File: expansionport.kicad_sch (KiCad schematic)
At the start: 0 parts

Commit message: place expansion port and set footprint
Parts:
- added J?: C64_Expansion_Port, HackupNet:C64-Cart-Socket-Vertical, symbol 00Project-TapePort:C64_Expansion_Port
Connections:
- new net +5V: J?.2 (Pin_2), J?.3 (Pin_3)
- new net A0: J?.Y (Pin_Y)
- new net A1: J?.X (Pin_X)
- new net A10: J?.M (Pin_M)
- new net A11: J?.L (Pin_L)
- new net A12: J?.K (Pin_K)
- new net A13: J?.J (Pin_J)
- new net A14: J?.H (Pin_H)
- new net A15: J?.F (Pin_F)
- new net A2: J?.W (Pin_W)
- new net A3: J?.V (Pin_V)
- new net A4: J?.U (Pin_U)
- new net A5: J?.T (Pin_T)
- new net A6: J?.S (Pin_S)
- new net A7: J?.R (Pin_R)
- new net A8: J?.P (Pin_P)
- new net A9: J?.N (Pin_N)
- new net BA: J?.12 (Pin_12)
- new net D0: J?.21 (Pin_21)
- new net D1: J?.20 (Pin_20)
- new net D2: J?.19 (Pin_19)
- new net D3: J?.18 (Pin_18)
- new net D4: J?.17 (Pin_17)
- new net D5: J?.16 (Pin_16)
- new net D6: J?.15 (Pin_15)
- new net D7: J?.14 (Pin_14)
- new net DMA_N: J?.13 (Pin_13)
- new net DOTCLOCK: J?.6 (Pin_6)
- new net EXROM_N: J?.9 (Pin_9)
- new net GAME_N: J?.8 (Pin_8)
- new net GND: J?.1 (Pin_1), J?.22 (Pin_22), J?.A (Pin_A), J?.Z (Pin_Z)
- new net IO1_N: J?.7 (Pin_7)
- new net IO2_N: J?.10 (Pin_10)
- new net IRQ_N: J?.4 (Pin_4)
- new net NMI_N: J?.D (Pin_D)
- new net PHI2: J?.E (Pin_E)
- new net RESET_N: J?.C (Pin_C)
- new net ROMH_N: J?.B (Pin_B)
- new net ROML_N: J?.11 (Pin_11)
- new net R_W: J?.5 (Pin_5)

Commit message: work on expansion port
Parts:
- added RN? (x4): 3.3K x 8, Resistor_THT:R_Array_SIP9, symbol Device:R_Network08
- added RN?: 4609X-AP1-332LF 3.3Kx8, Resistor_THT:R_Array_SIP9, symbol Device:R_Network08
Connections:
- net +5V: now also RN?.1 (common), RN?.1 (common), RN?.1 (common), RN?.1 (common), RN?.1 (common)
- net A0: now also RN?.9 (R8)
- net A1: now also RN?.8 (R7)
- net A10: now also RN?.7 (R6)
- net A11: now also RN?.6 (R5)
- net A12: now also RN?.5 (R4)
- net A13: now also RN?.4 (R3)
- net A14: now also RN?.3 (R2)
- net A15: now also RN?.2 (R1)
- net A2: now also RN?.7 (R6)
- net A3: now also RN?.6 (R5)
- net A4: now also RN?.5 (R4)
- net A5: now also RN?.4 (R3)
- net A6: now also RN?.3 (R2)
- net A7: now also RN?.2 (R1)
- net A8: now also RN?.9 (R8)
- net A9: now also RN?.8 (R7)
- net BA: now also RN?.9 (R8)
- net D0: now also RN?.2 (R1)
- net D1: now also RN?.3 (R2)
- net D2: now also RN?.4 (R3)
- net D3: now also RN?.5 (R4)
- net D4: now also RN?.6 (R5)
- net D5: now also RN?.7 (R6)
- net D6: now also RN?.8 (R7)
- net D7: now also RN?.9 (R8)
- net DMA_N: now also RN?.8 (R7)
- net EXROM_N: now also RN?.4 (R3)
- net GAME_N: now also RN?.5 (R4)
- net IO1_N: now also RN?.6 (R5)
- net IO2_N: now also RN?.3 (R2)
- net IRQ_N: now also RN?.9 (R8)
- net NMI_N: now also RN?.5 (R4)
- net PHI2: now also RN?.4 (R3)
- net RESET_N: now also RN?.6 (R5)
- net ROMH_N: now also RN?.7 (R6)
- net ROML_N: now also RN?.2 (R1)
- net R_W: now also RN?.8 (R7)
- no-connect marks 0 -> 3
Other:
- note added: "DOTCLOCK is directly from the FPGA through a level converter only, to get the required speed. All other signals, including CLK and R/W can be driven through the MUX bus. CLK, R_W, ROMH, ROML, IO1 and IO2 should be driven simultaneously to ensure clean address decoding."
- note added: "DOTCLOCK, IO1_N, IO2_N, ROML_N, ROMH_N, BA, PHI2 are all output only, and expect CMOS signals. IRQ_N, GAME_N, EXROM_N, NMI_N, DMA_N, RESET_N are all input only. IRQ, NMI and R/W can be open-collector outputs, with 3.3K pull-ups to match the C64. Thus we can use our normal mux latching with those signals. D0-7 and A0-15 are bidirectional, but direction switched as two banks. These can use 74LS244s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"

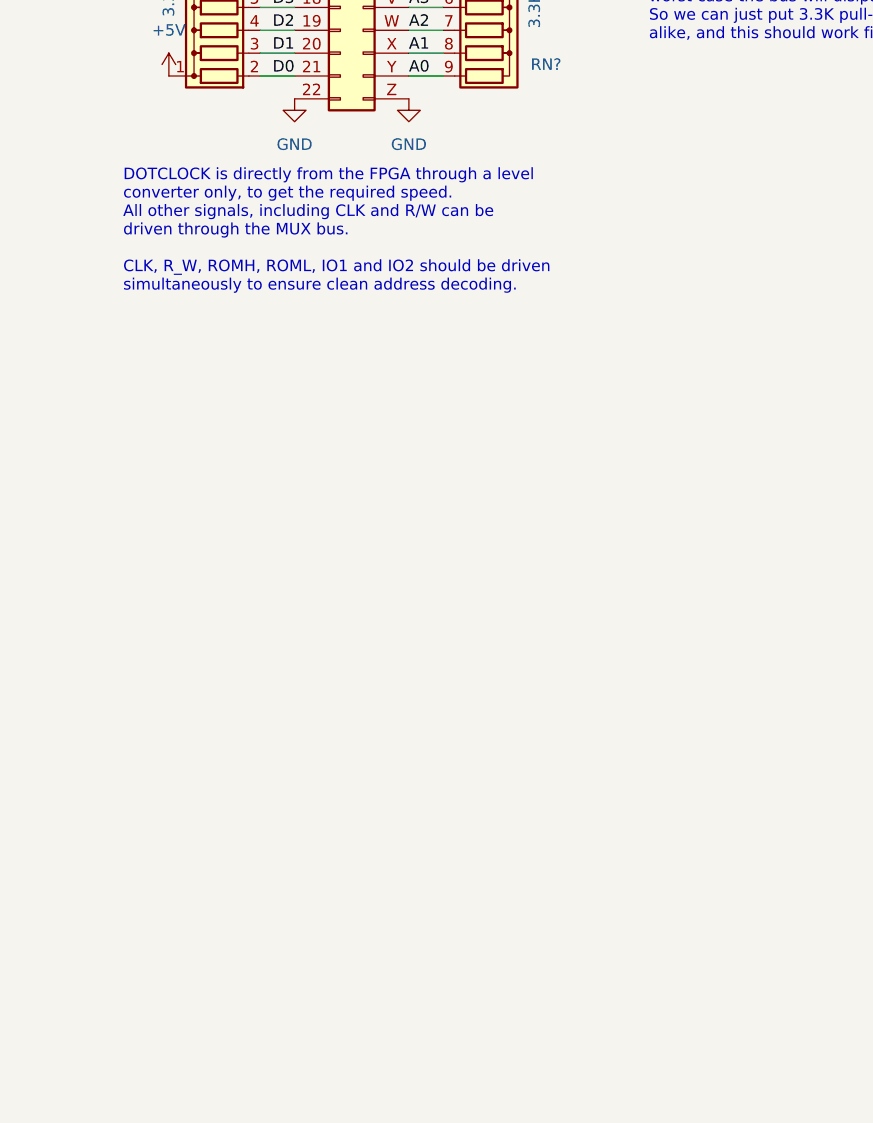
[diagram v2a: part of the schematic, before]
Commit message: DOTCLOCK fed via 74LS04 to perform fast level conversion
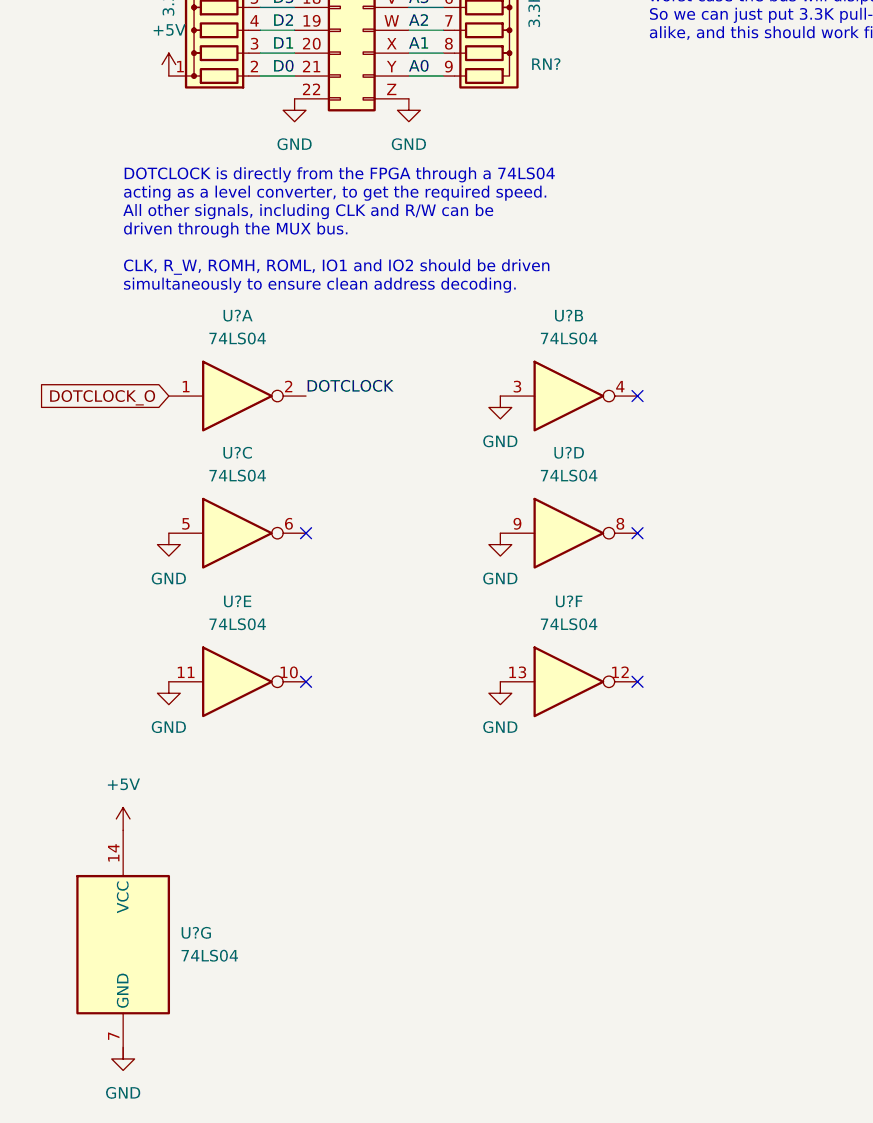
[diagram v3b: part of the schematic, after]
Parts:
- added U? (x7): 74LS04, symbol 74xx:74LS04
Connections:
- net +5V: now also U?.14 (VCC)
- net DOTCLOCK: now also U?.2
- net GND: now also U?.11, U?.13, U?.3, U?.5, U?.9
- new net DOTCLOCK_O: U?.1
- no-connect marks 3 -> 8
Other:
- note added: "DOTCLOCK is directly from the FPGA through a 74LS04 acting as a level converter, to get the required speed. All other signals, including CLK and R/W can be driven through the MUX bus. CLK, R_W, ROMH, ROML, IO1 and IO2 should be driven simultaneously to ensure clean address decoding."
- note removed: "DOTCLOCK is directly from the FPGA through a level converter only, to get the required speed. All other signals, including CLK and R/W can be driven through the MUX bus. CLK, R_W, ROMH, ROML, IO1 and IO2 should be driven simultaneously to ensure clean address decoding."

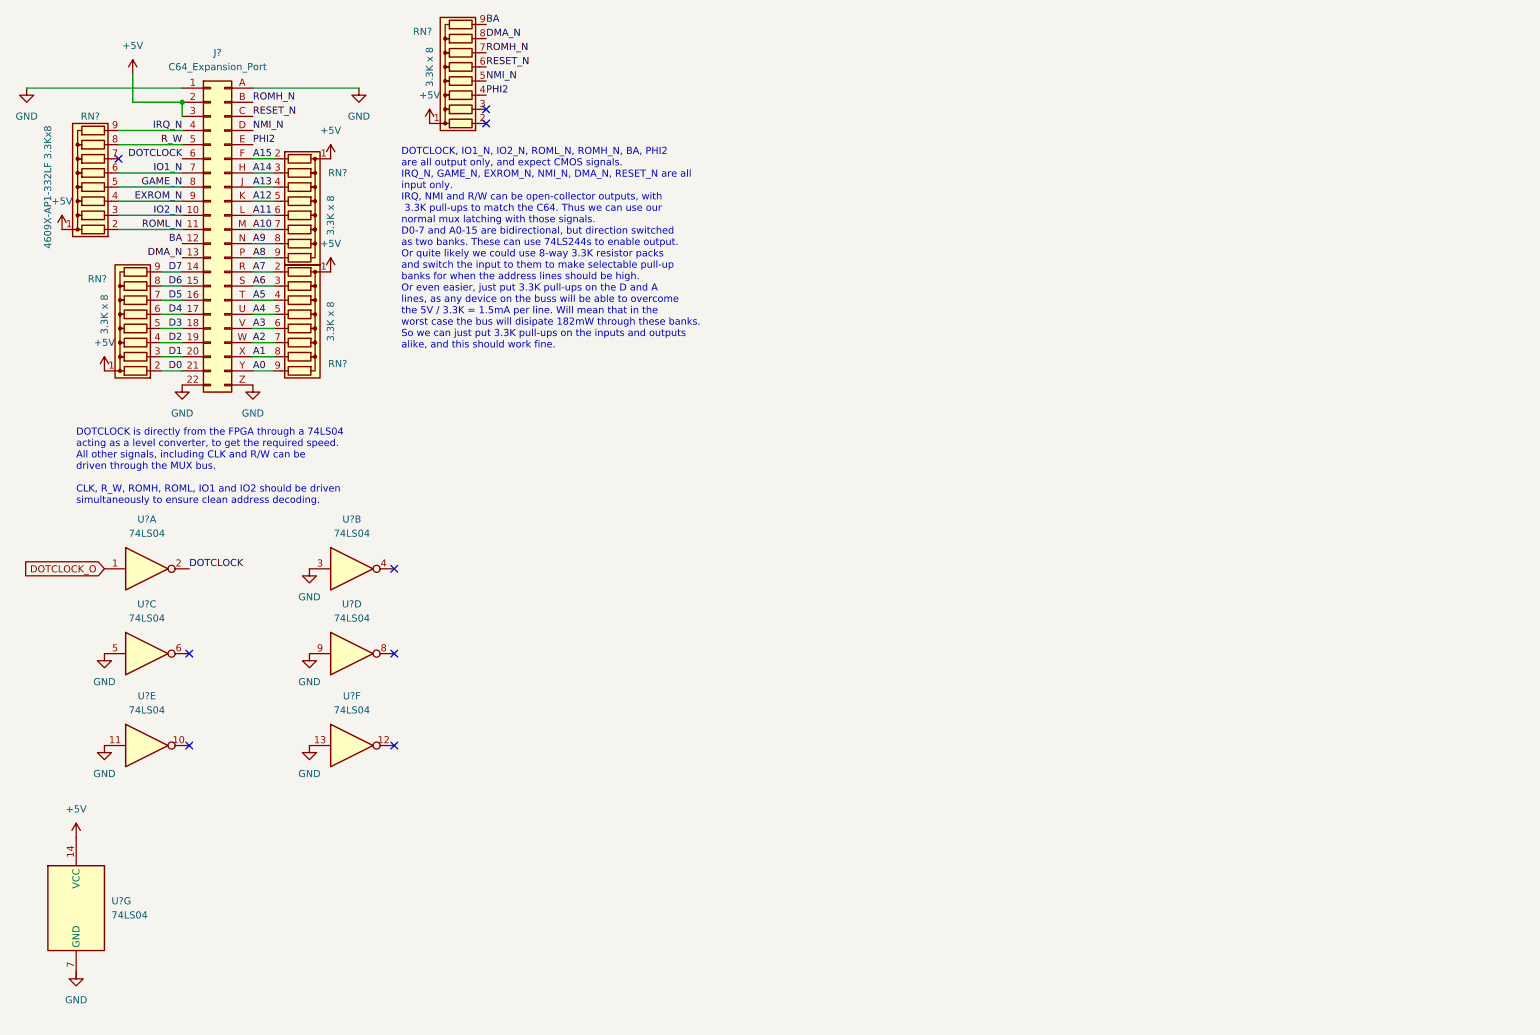
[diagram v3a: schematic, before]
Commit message: hook up expansion port using MUX bus
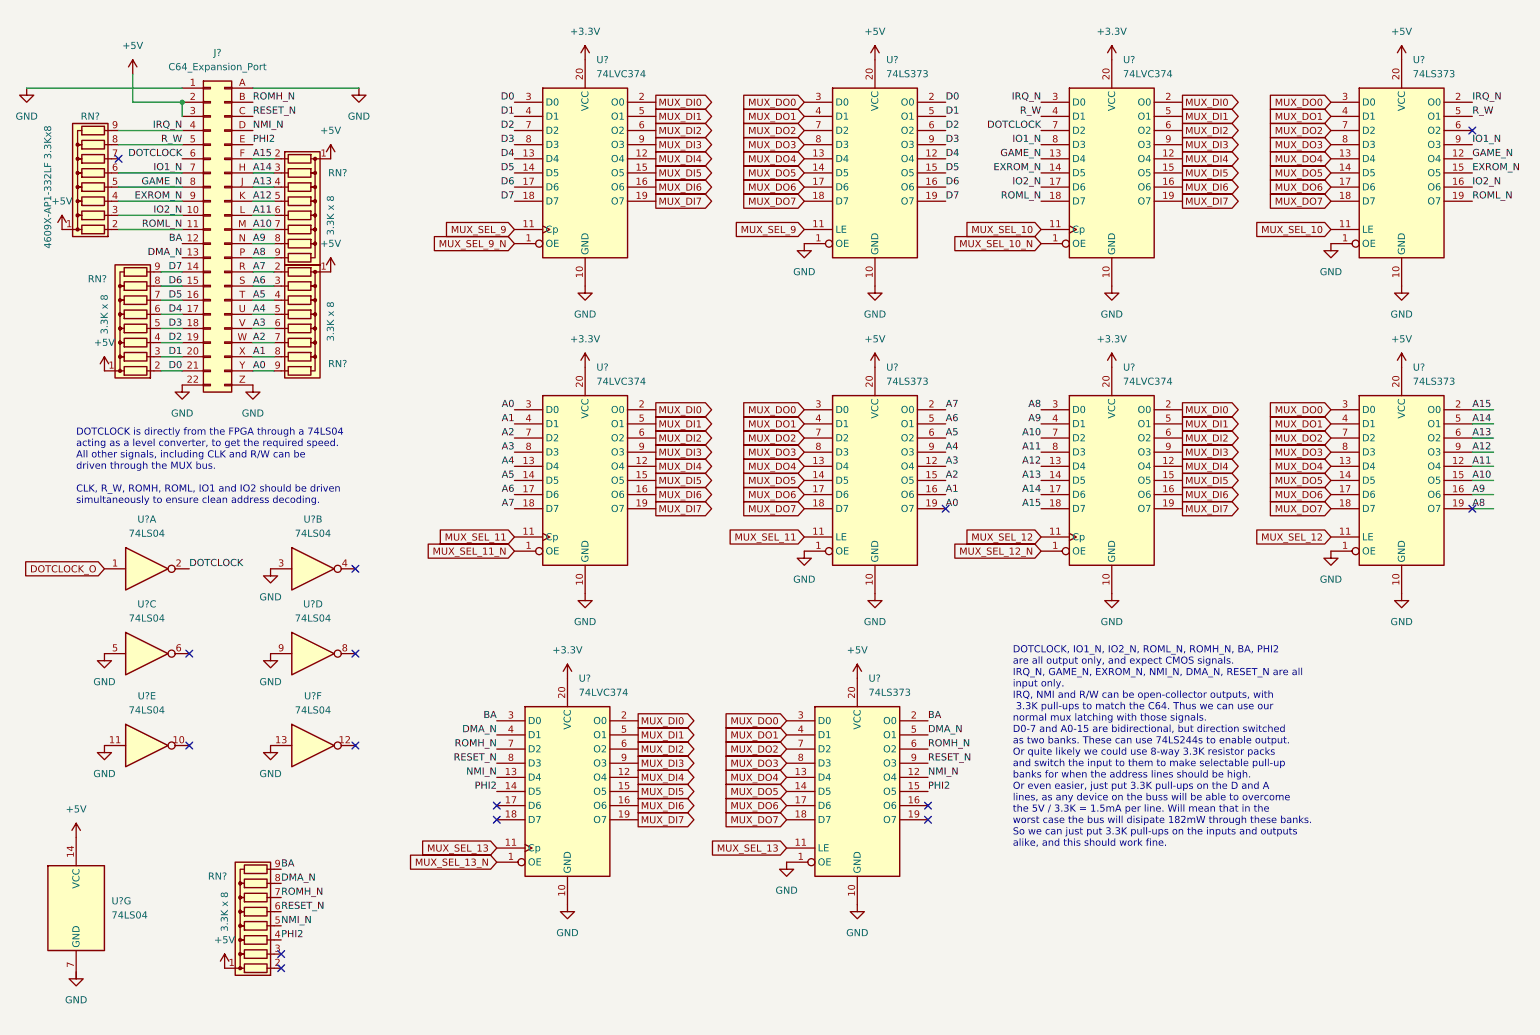
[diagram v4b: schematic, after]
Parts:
- added U? (x5): 74LS373, Package_DIP:DIP-20_W7.62mm, symbol 74xx:74LS373
- added U? (x5): 74LVC374, Package_DIP:DIP-20_W7.62mm, symbol 74xx:74HC374
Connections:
- net +5V: now also U?.20 (VCC), U?.20 (VCC), U?.20 (VCC), U?.20 (VCC), U?.20 (VCC)
- net A0: now also U?.19 (O7), U?.3 (D0)
- net A1: now also U?.16 (O6), U?.4 (D1)
- net A10: now also U?.15 (O5), U?.7 (D2)
- net A11: now also U?.12 (O4), U?.8 (D3)
- net A12: now also U?.13 (D4), U?.9 (O3)
- net A13: now also U?.14 (D5), U?.6 (O2)
- net A14: now also U?.17 (D6), U?.5 (O1)
- net A15: now also U?.18 (D7), U?.2 (O0)
- net A2: now also U?.15 (O5), U?.7 (D2)
- net A3: now also U?.12 (O4), U?.8 (D3)
- net A4: now also U?.13 (D4), U?.9 (O3)
- net A5: now also U?.14 (D5), U?.6 (O2)
- net A6: now also U?.17 (D6), U?.5 (O1)
- net A7: now also U?.18 (D7), U?.2 (O0)
- net A8: now also U?.19 (O7), U?.3 (D0)
- net A9: now also U?.16 (O6), U?.4 (D1)
- net BA: now also U?.2 (O0), U?.3 (D0)
- net D0: now also U?.2 (O0), U?.3 (D0)
- net D1: now also U?.4 (D1), U?.5 (O1)
- net D2: now also U?.6 (O2), U?.7 (D2)
- net D3: now also U?.8 (D3), U?.9 (O3)
- net D4: now also U?.12 (O4), U?.13 (D4)
- net D5: now also U?.14 (D5), U?.15 (O5)
- net D6: now also U?.16 (O6), U?.17 (D6)
- net D7: now also U?.18 (D7), U?.19 (O7)
- net DMA_N: now also U?.4 (D1), U?.5 (O1)
- net DOTCLOCK: now also U?.7 (D2)
- net EXROM_N: now also U?.14 (D5), U?.15 (O5)
- net GAME_N: now also U?.12 (O4), U?.13 (D4)
- net GND: now also U?.1 (OE), U?.1 (OE), U?.1 (OE), U?.1 (OE), U?.1 (OE), U?.10 (GND), U?.10 (GND), U?.10 (GND), U?.10 (GND), U?.10 (GND), U?.10 (GND), U?.10 (GND), U?.10 (GND), U?.10 (GND), U?.10 (GND)
- net IO1_N: now also U?.8 (D3), U?.9 (O3)
- net IO2_N: now also U?.16 (O6), U?.17 (D6)
- net IRQ_N: now also U?.2 (O0), U?.3 (D0)
- net NMI_N: now also U?.12 (O4), U?.13 (D4)
- net PHI2: now also U?.14 (D5), U?.15 (O5)
- net RESET_N: now also U?.8 (D3), U?.9 (O3)
- net ROMH_N: now also U?.6 (O2), U?.7 (D2)
- net ROML_N: now also U?.18 (D7), U?.19 (O7)
- net R_W: now also U?.4 (D1), U?.5 (O1)
- new net +3V3: U?.20 (VCC), U?.20 (VCC), U?.20 (VCC), U?.20 (VCC), U?.20 (VCC)
- new net MUX_DI0: U?.2 (O0), U?.2 (O0), U?.2 (O0), U?.2 (O0), U?.2 (O0)
- new net MUX_DI1: U?.5 (O1), U?.5 (O1), U?.5 (O1), U?.5 (O1), U?.5 (O1)
- new net MUX_DI2: U?.6 (O2), U?.6 (O2), U?.6 (O2), U?.6 (O2), U?.6 (O2)
- new net MUX_DI3: U?.9 (O3), U?.9 (O3), U?.9 (O3), U?.9 (O3), U?.9 (O3)
- new net MUX_DI4: U?.12 (O4), U?.12 (O4), U?.12 (O4), U?.12 (O4), U?.12 (O4)
- new net MUX_DI5: U?.15 (O5), U?.15 (O5), U?.15 (O5), U?.15 (O5), U?.15 (O5)
- new net MUX_DI6: U?.16 (O6), U?.16 (O6), U?.16 (O6), U?.16 (O6), U?.16 (O6)
- new net MUX_DI7: U?.19 (O7), U?.19 (O7), U?.19 (O7), U?.19 (O7), U?.19 (O7)
- new net MUX_DO0: U?.3 (D0), U?.3 (D0), U?.3 (D0), U?.3 (D0), U?.3 (D0)
- new net MUX_DO1: U?.4 (D1), U?.4 (D1), U?.4 (D1), U?.4 (D1), U?.4 (D1)
- new net MUX_DO2: U?.7 (D2), U?.7 (D2), U?.7 (D2), U?.7 (D2), U?.7 (D2)
- new net MUX_DO3: U?.8 (D3), U?.8 (D3), U?.8 (D3), U?.8 (D3), U?.8 (D3)
- new net MUX_DO4: U?.13 (D4), U?.13 (D4), U?.13 (D4), U?.13 (D4), U?.13 (D4)
- new net MUX_DO5: U?.14 (D5), U?.14 (D5), U?.14 (D5), U?.14 (D5), U?.14 (D5)
- new net MUX_DO6: U?.17 (D6), U?.17 (D6), U?.17 (D6), U?.17 (D6), U?.17 (D6)
- new net MUX_DO7: U?.18 (D7), U?.18 (D7), U?.18 (D7), U?.18 (D7), U?.18 (D7)
- new net MUX_SEL_10: U?.11 (Cp), U?.11 (LE)
- new net MUX_SEL_10_N: U?.1 (OE)
- new net MUX_SEL_11: U?.11 (Cp), U?.11 (LE)
- new net MUX_SEL_11_N: U?.1 (OE)
- new net MUX_SEL_12: U?.11 (Cp), U?.11 (LE)
- new net MUX_SEL_12_N: U?.1 (OE)
- new net MUX_SEL_13: U?.11 (Cp), U?.11 (LE)
- new net MUX_SEL_13_N: U?.1 (OE)
- new net MUX_SEL_9: U?.11 (Cp), U?.11 (LE)
- new net MUX_SEL_9_N: U?.1 (OE)
- no-connect marks 8 -> 15
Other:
- moved on the sheet: RN?, U?B, U?D, U?F

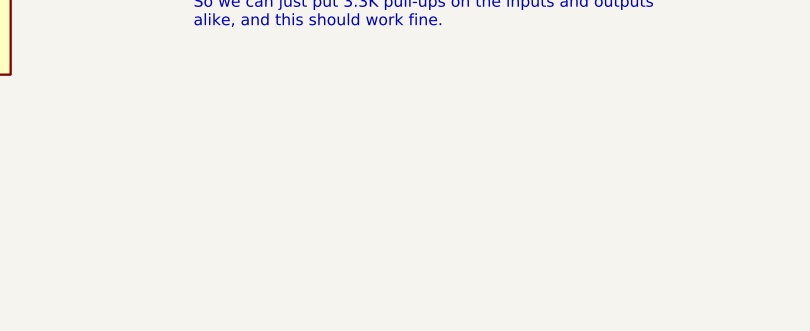
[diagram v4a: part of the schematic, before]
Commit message: beautify the schematics, especially the title-page
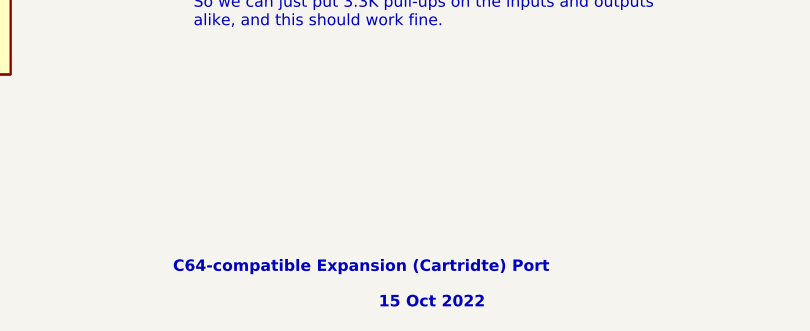
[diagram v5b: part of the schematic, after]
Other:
- note added: "15 Oct 2022"
- note added: "C64-compatible Expansion (Cartridte) Port"
